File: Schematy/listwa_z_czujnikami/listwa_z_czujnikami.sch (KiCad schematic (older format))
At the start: 25 parts, among them P1 CONN_01X10, U1 KTIR0711S, U2 KTIR0711S, U3 KTIR0711S, U4 KTIR0711S, U5 KTIR0711S, U6 KTIR0711S, U7 KTIR0711S, U8 KTIR0711S

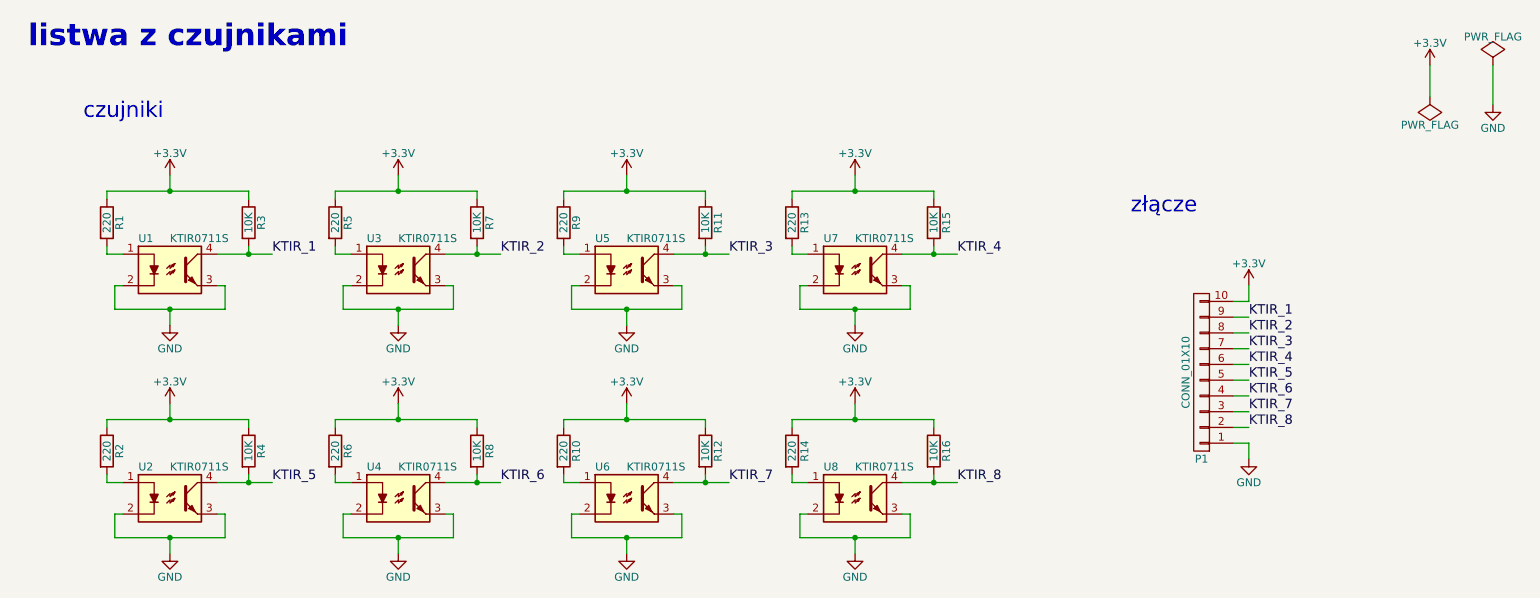
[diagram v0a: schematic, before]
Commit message: Kompletny schemat elektryczny [do sprawdzenia]
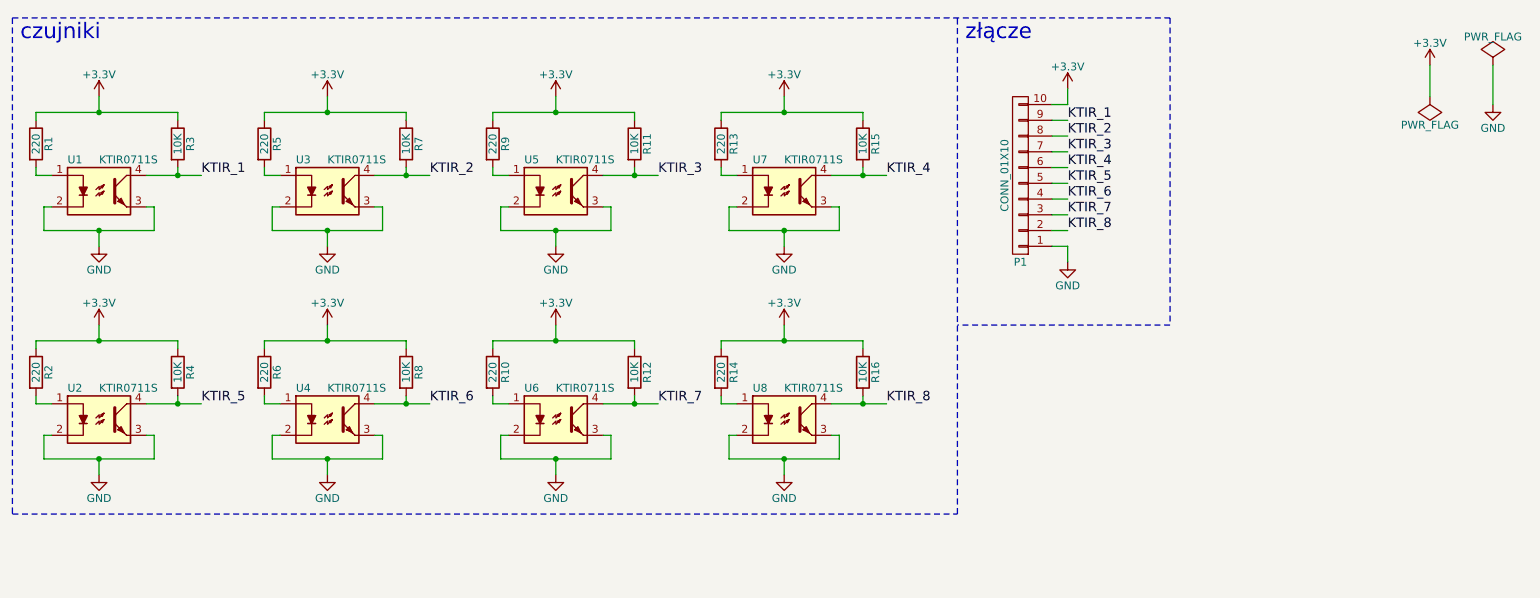
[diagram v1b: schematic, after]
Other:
- note removed: "listwa z czujnikami"
- moved on the sheet: P1, R1, R10, R11, R12, R13, R14, R15, R16, R2, R3, R4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
